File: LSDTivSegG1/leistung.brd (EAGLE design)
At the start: 160 x 100 mm, 58 parts, among them IC1 IR2184D, IC2 IR2184D, IC3 IR2184D, IC4 4081N, IC5 4069N, IC6 IR2184D, X1 057-010-1, X2 MKDSN1,5/2-5,08

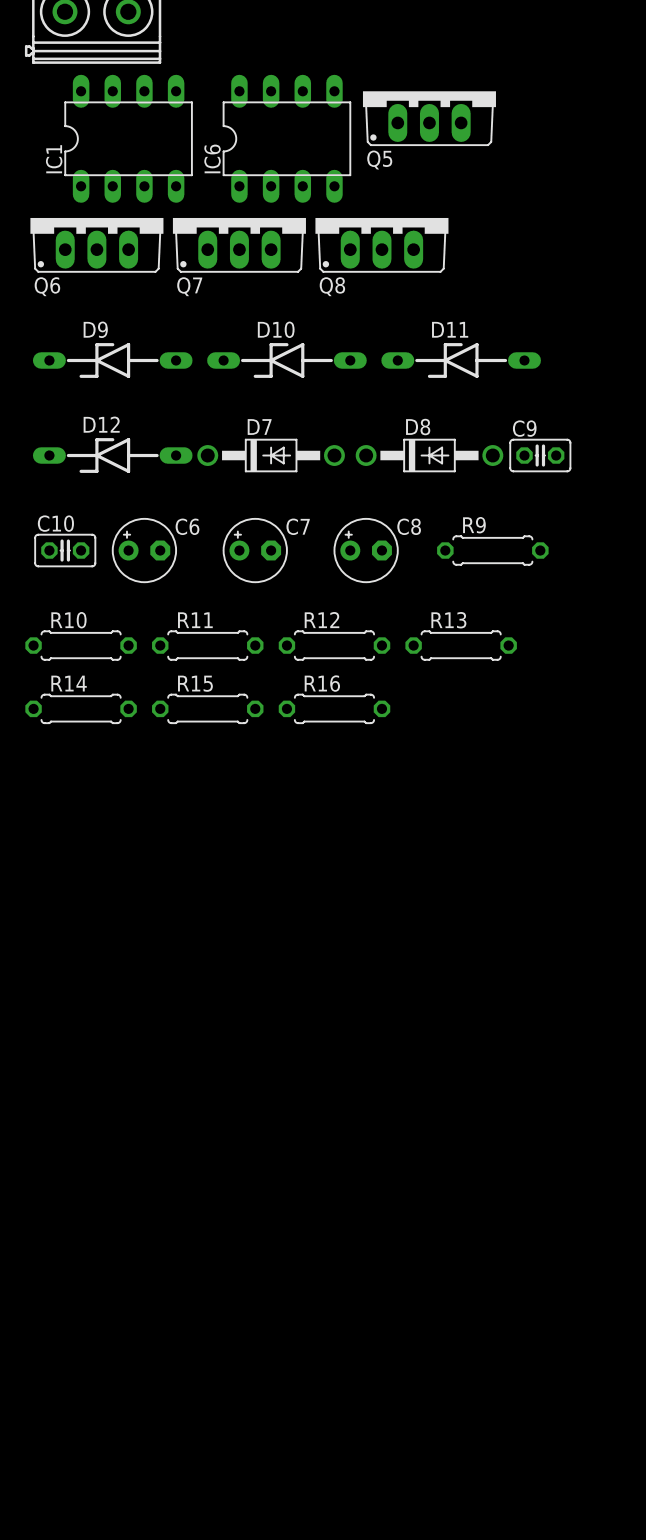
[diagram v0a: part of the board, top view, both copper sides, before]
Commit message: changed naming high/low voltage area
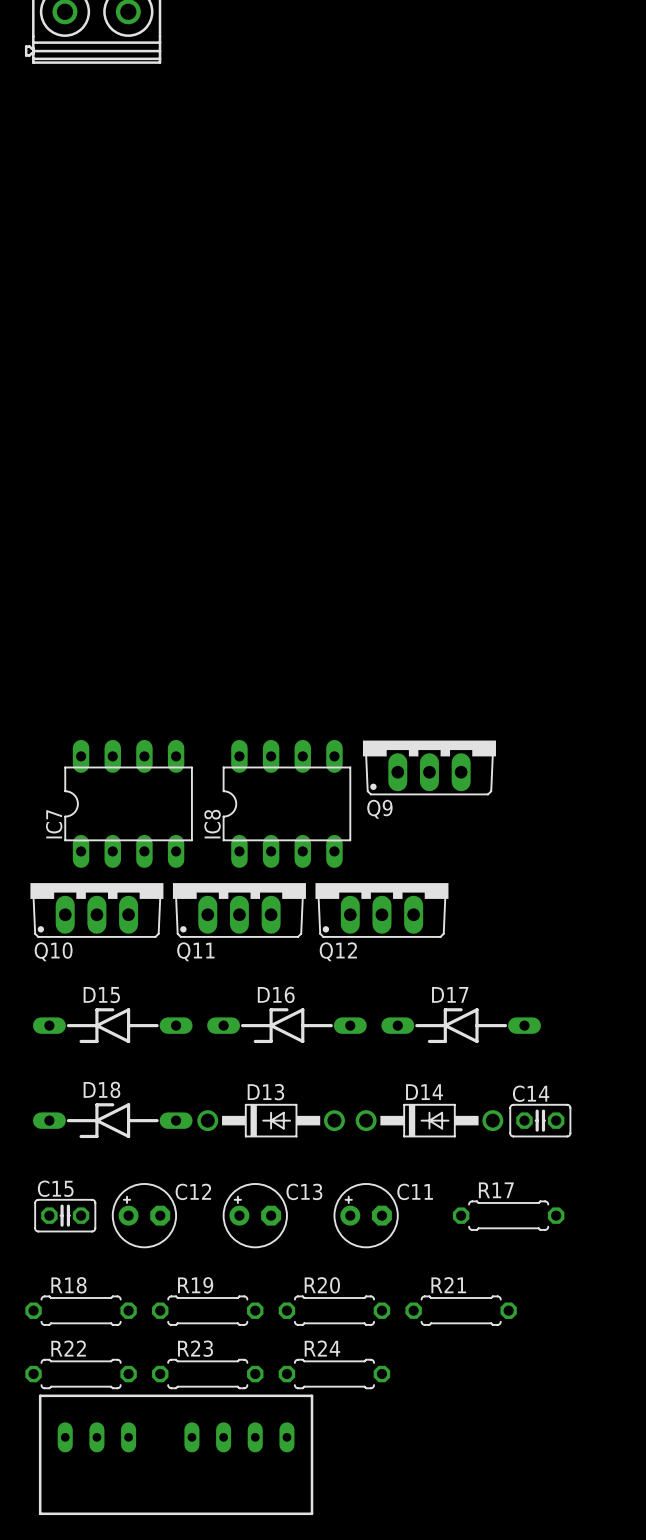
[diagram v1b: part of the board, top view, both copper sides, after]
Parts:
- removed C10, C9: 100n, rcl:C025-025X050
- removed C6: 10u, rcl:E2,5-5
- removed C7, C8: 1u, rcl:E2,5-5
- removed D10, D11, D12, D9: 18, diode:ZDIO-10
- removed D7, D8: 1N4001, diode:DO41-10
- removed IC1, IC6: IR2184D, irs:DIL08
- removed Q5, Q6, Q7, Q8: (no value), transistor-power:TO220BV
- removed R10, R11, R12, R9: 10, rcl:0207/7
- removed R13, R14, R15, R16: 47k, rcl:0207/7
- added C11: 10u, rcl:E2,5-5
- added C12, C13: 1u, rcl:E2,5-5
- added C14, C15: 100n, rcl:C025-025X050
- added D13, D14: 1N4001, diode:DO41-10
- added D15, D16, D17, D18: 18, diode:ZDIO-10
- added DC1: TMR, traco_tmr:TRACO_SIP-8
- added IC7, IC8: IR2184D, irs:DIL08
- added Q10, Q11, Q12, Q9: (no value), transistor-power:TO220BV
- added R17, R18, R19, R20: 10, rcl:0207/7
- added R21, R22, R23, R24: 47k, rcl:0207/7
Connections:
- net BAT_PWM_OUT renamed BAT_PWM_OUT_CTL
- removed net 5V_OUT: X1.1
- removed net GND_OUT: X1.3
- removed net N$13: D10.C, Q6.G, R10.2, R15.1
- removed net N$14: D9.C, Q5.G, R16.2, R9.2
- removed net N$17: D12.C, Q7.G, R12.1, R13.2
- removed net N$18: D11.C, Q8.G, R11.1, R14.1
- removed net N$25: IC1.4, R10.1
- removed net N$26: IC1.7, R9.1
- removed net N$27: IC6.7, R12.2
- removed net N$28: IC6.4, R11.2
- new net 5V_OUT_CTL: DC1.6, X1.1
- new net DIRL_IN_CTL: X1.5
- new net DIRR_INV: IC8.1
- new net DIRR_IN_CTL: X1.7
- new net ENABLE_CTL: X1.9
- new net GND_OUT_CTL: DC1.7, X1.3
- new net MOTOR_PWM_L_CTL: X1.2
- new net MOTOR_PWM_R_CTL: X1.4
- new net N$29: D16.C, Q10.G, R18.2, R23.1
- new net N$30: D15.C, Q9.G, R17.2, R24.2
- new net N$31: D18.C, Q11.G, R20.1, R21.2
- new net N$32: D17.C, Q12.G, R19.1, R22.1
- new net N$33: IC7.4, R18.1
- new net N$34: IC7.7, R17.1
- new net N$35: IC8.7, R20.2
- new net N$36: IC8.4, R19.2
- net +15V: now also C14.1, C15.1, D13.A, D14.A, IC7.5, IC8.5; no longer C10.1, C9.1, D7.A, D8.A, IC1.5, IC6.5
- net +24V: now also DC1.2
- net BAT_+: now also C11.+, Q11.D, Q9.D; no longer C6.+, Q5.D, Q7.D
- net BAT_-: now also C11.-, C14.2, C15.2, DC1.1, IC7.3, IC8.3, Q10.S, Q12.S; no longer C10.2, C6.-, C9.2, IC1.3, IC6.3, Q6.S, Q8.S
- net DIRL_IN: no longer IC1.1, X1.5
- net DIRL_INV: no longer IC6.1
- net DIRR_IN: now also IC7.1; no longer X1.7
- net ENABLE: no longer X1.9
- net MOTOR_L_+: no longer C7.-, D10.A, D9.A, IC1.6, Q5.S, Q6.D, R15.2, R16.1
- net MOTOR_L_-: no longer C8.-, D11.A, D12.A, IC6.6, Q7.S, Q8.D, R13.1, R14.2
- net MOTOR_L_ACTIVE: no longer IC1.2, IC6.2
- net MOTOR_PWM_L: no longer X1.2
- net MOTOR_PWM_R: no longer X1.4
- net MOTOR_R_+: now also C12.-, D15.A, D16.A, IC7.6, Q10.D, Q9.S, R23.2, R24.1
- net MOTOR_R_-: now also C13.-, D17.A, D18.A, IC8.6, Q11.S, Q12.D, R21.1, R22.2
- net MOTOR_R_ACTIVE: now also IC7.2, IC8.2
- net VB: now also C12.+, C13.+, D13.C, D14.C, IC7.8, IC8.8; no longer C7.+, C8.+, D7.C, D8.C, IC1.8, IC6.8

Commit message: added supply to logic gates
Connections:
- removed net N$1: IC4.14
- removed net N$2: IC4.7
- removed net N$3: IC5.14
- removed net N$4: IC5.7
- new net +5V: IC4.14, IC5.14
- new net GND: IC4.7, IC5.7
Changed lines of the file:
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@@
 <layer number="51" name="tDocu" color="7" fill="1" visible="yes" active="yes"/>
 <layer number="52" name="bDocu" color="7" fill="1" visible="yes" active="yes"/>
+<layer number="53" name="tGND_GNDA" color="7" fill="9" visible="no" active="no"/>
+<layer number="54" name="bGND_GNDA" color="1" fill="9" visible="no" active="no"/>
 <layer number="56" name="wert" color="7" fill="1" visible="no" active="no"/>
 <layer number="88" name="SimResults" color="9" fill="1" visible="no" active="no"/>
@@
 <layer number="101" name="Gehäuse" color="7" fill="1" visible="yes" active="yes"/>
 <layer number="102" name="Mittellin" color="7" fill="1" visible="yes" active="yes"/>
+<layer number="103" name="tMap" color="7" fill="1" visible="no" active="yes"/>
 <layer number="104" name="Name" color="7" fill="1" visible="yes" active="yes"/>
+<layer number="105" name="tPlate" color="7" fill="1" visible="no" active="yes"/>
+<layer number="106" name="bPlate" color="7" fill="1" visible="no" active="yes"/>
+<layer number="107" name="Crop" color="7" fill="1" visible="no" active="yes"/>
+<layer number="116" name="Patch_BOT" color="9" fill="4" visible="no" active="yes"/>
+<layer number="121" name="_tsilk" color="7" fill="1" visible="no" active="yes"/>
+<layer number="122" name="_bsilk" color="7" fill="1" visible="no" active="yes"/>
+<layer number="125" name="_tNames" color="7" fill="1" visible="no" active="yes"/>
+<layer number="144" name="Drill_legend" color="7" fill="1" visible="no" active="yes"/>
 <layer number="151" name="HeatSink" color="7" fill="1" visible="yes" active="yes"/>
+<layer number="199" name="Contour" color="7" fill="1" visible="no" active="yes"/>
 <layer number="200" name="200bmp" color="1" fill="10" visible="no" active="no"/>
+<layer number="201" name="201bmp" color="2" fill="10" visible="no" active="yes"/>
+<layer number="202" name="202bmp" color="3" fill="10" visible="no" active="yes"/>
+<layer number="203" name="203bmp" color="4" fill="10" visible="no" active="yes"/>
+<layer number="204" name="204bmp" color="5" fill="10" visible="no" active="yes"/>
+<layer number="205" name="205bmp" color="6" fill="10" visible="no" active="yes"/>
+<layer number="206" name="206bmp" color="7" fill="10" visible="no" active="yes"/>
+<layer number="207" name="207bmp" color="8" fill="10" visible="no" active="yes"/>
+<layer number="208" name="208bmp" color="9" fill="10" visible="no" active="yes"/>
+<layer number="209" name="209bmp" color="7" fill="1" visible="no" active="yes"/>
+<layer number="210" name="210bmp" color="7" fill="1" visible="no" active="yes"/>
+<layer number="211" name="211bmp" color="7" fill="1" visible="no" active="yes"/>
+<layer number="212" name="212bmp" color="7" fill="1" visible="no" active="yes"/>
+<layer number="213" name="213bmp" color="7" fill="1" visible="no" active="yes"/>
+<layer number="214" name="214bmp" color="7" fill="1" visible="no" active="yes"/>
+<layer number="215" name="215bmp" color="7" fill="1" visible="no" active="yes"/>
+<layer number="216" name="216bmp" color="7" fill="1" visible="no" active="yes"/>
+<layer number="217" name="217bmp" color="18" fill="1" visible="no" active="no"/>
+<layer number="218" name="218bmp" color="19" fill="1" visible="no" active="no"/>
+<layer number="219" name="219bmp" color="20" fill="1" visible="no" active="no"/>
+<layer number="220" name="220bmp" color="21" fill="1" visible="no" active="no"/>
+<layer number="221" name="221bmp" color="22" fill="1" visible="no" active="no"/>
+<layer number="222" name="222bmp" color="23" fill="1" visible="no" active="no"/>
+<layer number="223" name="223bmp" color="24" fill="1" visible="no" active="no"/>
+<layer number="224" name="224bmp" color="25" fill="1" visible="no" active="no"/>
 <layer number="250" name="Descript" color="3" fill="1" visible="no" active="no"/>
 <layer number="251" name="SMDround" color="12" fill="11" visible="no" active="no"/>
@@
 <contactref element="IC3" pad="1"/>
 </signal>
-<signal name="N$1">
-<contactref element="IC4" pad="14"/>
-</signal>
-<signal name="N$2">
-<contactref element="IC4" pad="7"/>
-</signal>
-<signal name="N$3">
-<contactref element="IC5" pad="14"/>
-</signal>
-<signal name="N$4">
-<contactref element="IC5" pad="7"/>
-</signal>
 <signal name="+24_HORN">
 <contactref element="F3" pad="2"/>
@@
 <contactref element="X1" pad="4"/>
 </signal>
+<signal name="+5V">
+<contactref element="IC4" pad="14"/>
+<contactref element="IC5" pad="14"/>
+<wire x1="-45.72" y1="-170.18" x2="-45.72" y2="-181.61" width="0" layer="19" extent="1-1"/>
+</signal>
+<signal name="GND">
+<contactref element="IC4" pad="7"/>
+<contactref element="IC5" pad="7"/>
+<wire x1="-30.48" y1="-177.8" x2="-30.48" y2="-189.23" width="0" layer="19" extent="1-1"/>
+</signal>
 </signals>

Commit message: merged alexs schmeatic with the one from dominik
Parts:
- added C10, C16: 100n, rcl:C025-025X050
- added C6: 1000u, rcl:E2,5-4R
- added C7: 100u, rcl:E2,5-4R
- added C8: 100u, rcl:E2,5-7
- added C9: 1000u, rcl:E5-13
- added D7: 1N 5711, diode:CB417-15
- added D8: 1N 5711, diode:CB429-15
- added IC1: LM 2576 T5,0, LM2576:TO-220-5_IN-LINE
- added IC10, IC11: LTV844, lsd2016:DIL16
- added IC6: LM 2576 T15, LM2576:TO-220-5_IN-LINE
- added IC9: TINY13-20PU, atmel:DIL08
- added L1, L2: 100u, rcl:0204/5
- added LED1, LED2: blau, led:LED3MM
- added R10: 16k, rcl:0207/10
- added R11, R12, R13, R25, R26, R27: 220, rcl:0207/10
- added R14: 100, rcl:0207/10
- added R15: 680, rcl:0207/10
- added R16: 82k, rcl:0207/10
- added R28, R29, R30, R31, R32, R33, R9: 10k, rcl:0207/10
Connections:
- new net ADC: IC9.3, R10.2, R16.1
- new net BAT_PWM_IN: IC9.5, R25.1
- new net MOTOR_PWN_L_CTL: R26.1
- new net N$1: D7.C, IC1.P$2, L1.1
- new net N$13: IC10.1, R11.2
- new net N$14: IC10.3, R12.2
- new net N$17: IC10.5, R13.2
- new net N$18: IC10.7, R25.2
- new net N$2: LED1.A, R14.1
- new net N$25: IC11.3, R27.2
- new net N$26: IC11.1, R26.2
- new net N$3: LED2.A, R15.2
- new net N$4: D8.C, IC6.P$2, L2.1
- new net RESET: C16.1, IC9.1, R9.2
- net +15V: now also C9.+, IC6.P$4, L2.2, R15.1
- net +24V: now also C7.+, C8.+, IC1.P$1, IC6.P$1, R16.2
- net +5V: now also C10.2, C6.+, IC1.P$4, IC9.8, L1.2, R14.2, R28.1, R29.1, R30.1, R32.1, R33.1, R9.1
- net 5V_OUT_CTL: now also R31.1
- net BAT_PWM_OUT_CTL: now also IC10.10, R31.2
- net DIRL_IN: now also IC10.16, R28.2
- net DIRL_IN_CTL: now also R11.1
- net DIRR_IN: now also IC10.14, R29.2
- net DIRR_IN_CTL: now also R12.1
- net ENABLE: now also IC10.12, R30.2
- net ENABLE_CTL: now also R13.1
- net GND: now also C10.1, C16.2, C6.-, C7.-, C8.-, C9.-, D7.A, D8.A, IC1.P$3, IC1.P$5, IC10.11, IC10.13, IC10.15, IC10.8, IC11.13, IC11.15, IC6.P$3, IC6.P$5, IC9.4, LED1.K, LED2.K, R10.1
- net GND_OUT_CTL: now also IC10.2, IC10.4, IC10.6, IC10.9, IC11.2, IC11.4
- net MOTOR_PWM_L: now also IC11.16, R32.2
- net MOTOR_PWM_R: now also IC11.14, R33.2
- net MOTOR_PWM_R_CTL: now also R27.1

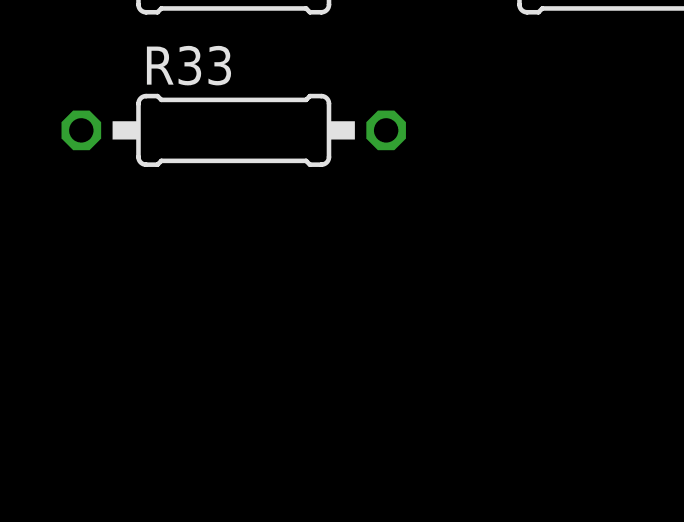
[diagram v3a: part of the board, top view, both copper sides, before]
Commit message: added 5V status led to LST side
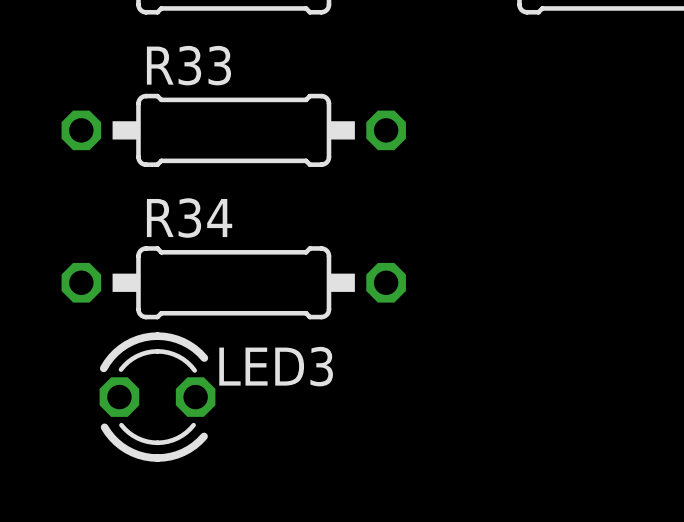
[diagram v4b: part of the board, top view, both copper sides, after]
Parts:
- added LED3: blau, led:LED3MM
- added R34: 100, rcl:0207/10
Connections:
- new net N$27: LED3.A, R34.1
- net 5V_OUT_CTL: now also R34.2
- net GND_OUT_CTL: now also LED3.K
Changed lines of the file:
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@@
 <element name="R32" library="rcl" package="0207/10" value="10k" x="-31.75" y="-501.65"/>
 <element name="R33" library="rcl" package="0207/10" value="10k" x="-44.45" y="-506.73"/>
+<element name="LED3" library="led" package="LED3MM" value="blau" x="-46.99" y="-515.62"/>
+<element name="R34" library="rcl" package="0207/10" value="100" x="-44.45" y="-511.81"/>
 </elements>
 <signals>
@@
 <contactref element="DC1" pad="6"/>
 <contactref element="R31" pad="1"/>
+<contactref element="R34" pad="2"/>
 <wire x1="-49.53" y1="-501.65" x2="-34.29" y2="-346.71" width="0" layer="19" extent="1-1"/>
+<wire x1="-39.37" y1="-511.81" x2="-49.53" y2="-501.65" width="0" layer="19" extent="1-1"/>
 <wire x1="-29.21" y1="53.34" x2="-34.29" y2="-346.71" width="0" layer="19" extent="1-1"/>
 </signal>
@@
 <contactref element="IC11" pad="2"/>
 <contactref element="IC11" pad="4"/>
+<contactref element="LED3" pad="K"/>
 <wire x1="-33.02" y1="-464.82" x2="-38.1" y2="-464.82" width="0" layer="19" extent="1-1"/>
 <wire x1="-43.18" y1="-464.82" x2="-38.1" y2="-464.82" width="0" layer="19" extent="1-1"/>
@@
 <wire x1="-43.18" y1="-476.25" x2="-43.18" y2="-464.82" width="0" layer="19" extent="1-1"/>
 <wire x1="-38.1" y1="-476.25" x2="-43.18" y2="-476.25" width="0" layer="19" extent="1-1"/>
+<wire x1="-45.72" y1="-515.62" x2="-43.18" y2="-476.25" width="0" layer="19" extent="1-1"/>
 <wire x1="-31.75" y1="-346.71" x2="-27.94" y2="-457.2" width="0" layer="19" extent="1-1"/>
 <wire x1="-26.67" y1="53.34" x2="-31.75" y2="-346.71" width="0" layer="19" extent="1-1"/>
@@
 <contactref element="R26" pad="1"/>
 </signal>
+<signal name="N$27">
+<contactref element="LED3" pad="A"/>
+<contactref element="R34" pad="1"/>
+<wire x1="-49.53" y1="-511.81" x2="-48.26" y2="-515.62" width="0" layer="19" extent="1-1"/>
+</signal>
 </signals>

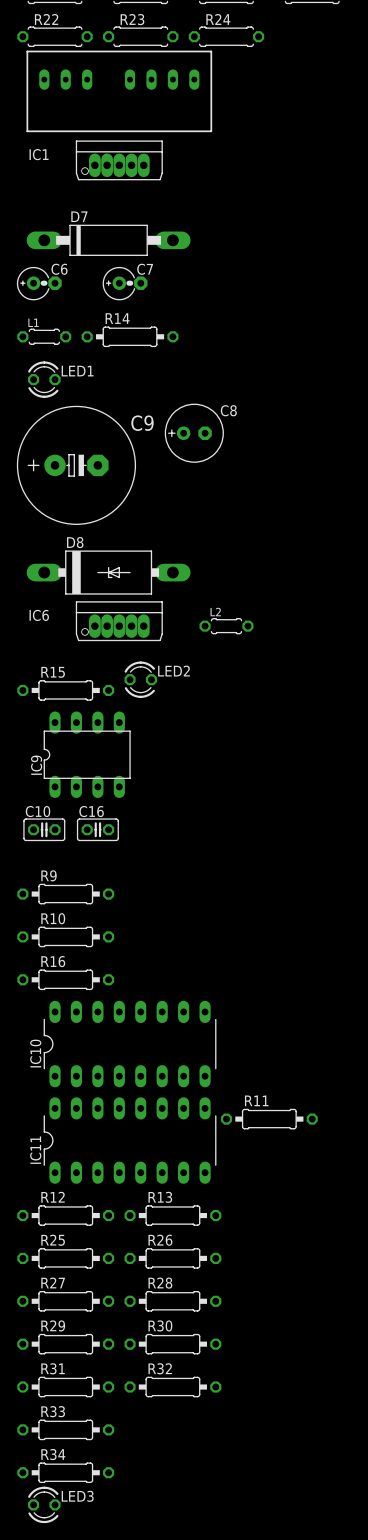
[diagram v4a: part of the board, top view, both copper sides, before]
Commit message: moved decoupling to regelungsplatine
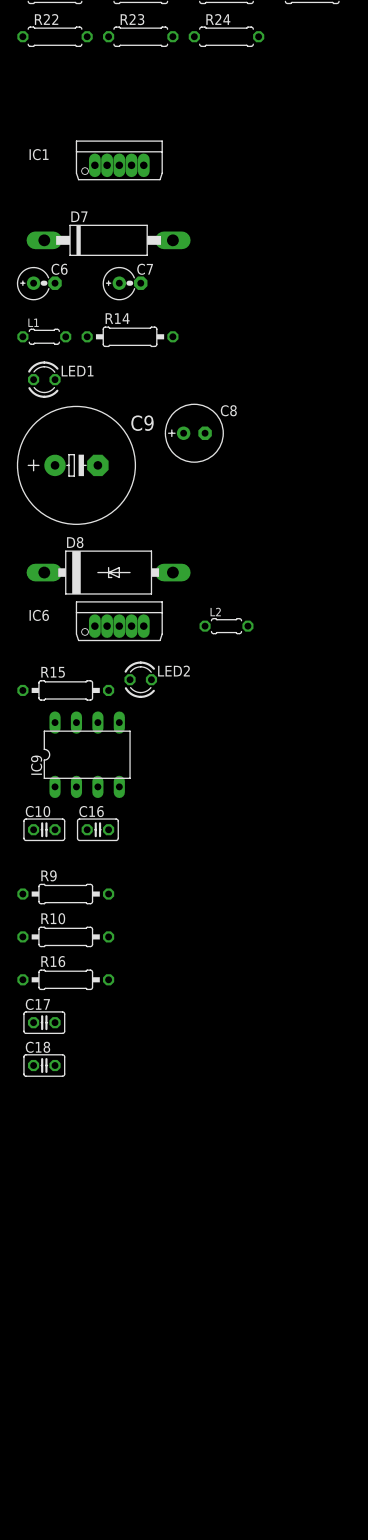
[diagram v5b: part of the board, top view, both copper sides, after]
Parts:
- removed DC1: TMR, traco_tmr:TRACO_SIP-8
- removed IC10, IC11: LTV844, lsd2016:DIL16
- removed LED3: blau, led:LED3MM
- removed R11, R12, R13, R25, R26, R27: 220, rcl:0207/10
- removed R28, R29, R30, R31, R32, R33: 10k, rcl:0207/10
- removed R34: 100, rcl:0207/10
- added C17, C18: 100nF, rcl:C025-025X050
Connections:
- removed net 5V_OUT_CTL: DC1.6, R31.1, R34.2, X1.1
- removed net BAT_-: C1.-, C11.-, C14.2, C15.2, C4.2, C5.2, DC1.1, IC2.3, IC3.3, IC7.3, IC8.3, Q10.S, Q12.S, Q3.S, Q4.S, U$1.4A, U$1.4B, X2.1
- removed net BAT_PWM_OUT_CTL: IC10.10, R31.2, X1.6
- removed net DIRL_IN: IC10.16, IC2.1, IC5.1, R28.2
- removed net DIRL_IN_CTL: R11.1, X1.5
- removed net DIRR_IN: IC10.14, IC5.3, IC7.1, R29.2
- removed net DIRR_IN_CTL: R12.1, X1.7
- removed net ENABLE_CTL: R13.1, X1.9
- removed net GND_OUT_CTL: DC1.7, IC10.2, IC10.4, IC10.6, IC10.9, IC11.2, IC11.4, LED3.K, X1.3
- removed net MOTOR_PWM_L_CTL: X1.2
- removed net MOTOR_PWM_R_CTL: R27.1, X1.4
- removed net MOTOR_PWN_L_CTL: R26.1
- removed net N$13: IC10.1, R11.2
- removed net N$14: IC10.3, R12.2
- removed net N$17: IC10.5, R13.2
- removed net N$18: IC10.7, R25.2
- removed net N$25: IC11.3, R27.2
- removed net N$26: IC11.1, R26.2
- removed net N$27: LED3.A, R34.1
- removed net NC: X1.8
- new net BAT_PWM: X1.6
- new net DIRL: IC2.1, IC5.1, X1.5
- new net DIRR: IC5.3, IC7.1, X1.7
- net +24V: now also X1.1; no longer DC1.2
- net +5V: now also C17.1, C18.1, X1.8; no longer R28.1, R29.1, R30.1, R32.1, R33.1
- net BAT_PWM_IN: no longer R25.1
- net ENABLE: now also X1.9; no longer IC10.12, R30.2
- net GND: now also C1.-, C11.-, C14.2, C15.2, C17.2, C18.2, C4.2, C5.2, IC2.3, IC3.3, IC7.3, IC8.3, Q10.S, Q12.S, Q3.S, Q4.S, U$1.4A, U$1.4B, X1.3, X2.1; no longer IC10.11, IC10.13, IC10.15, IC10.8, IC11.13, IC11.15
- net MOTOR_PWM_L: now also X1.2; no longer IC11.16, R32.2
- net MOTOR_PWM_R: now also X1.4; no longer IC11.14, R33.2
